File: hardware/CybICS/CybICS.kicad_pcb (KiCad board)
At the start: 2 copper layers, 160 x 100 mm, 17 parts, among them J1 Raspberry_Pi_2_3, U1 STM32G070RBTx

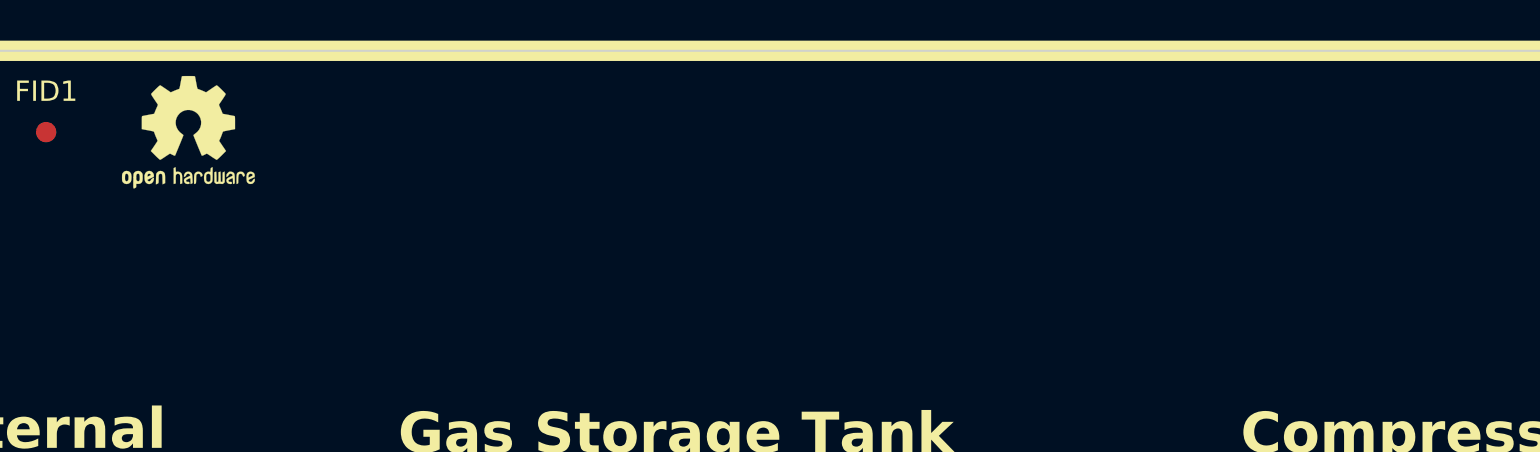
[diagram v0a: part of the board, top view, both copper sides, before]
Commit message: Fixed footprint
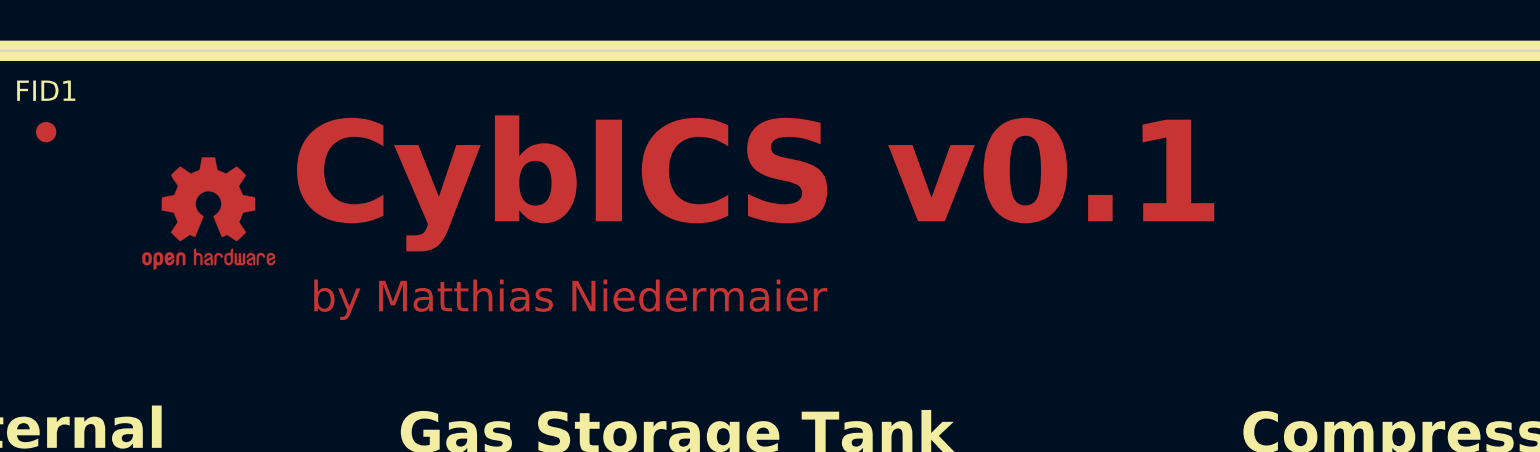
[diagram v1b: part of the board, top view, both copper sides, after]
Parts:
- moved #SYM1 4.12 mm to (66.8, 58.8)
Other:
- board text added: "CybICS v0.1"
- board text added: "by Matthias Niedermaier"

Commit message: Further development of the schematic and pcb
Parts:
- added C1: 100nF, Capacitor_SMD:C_0805_2012Metric_Pad1.18x1.45mm_HandSolder, F.Cu at (84.5, 121.5)
- added C2: 100nF, Capacitor_SMD:C_0805_2012Metric_Pad1.18x1.45mm_HandSolder, F.Cu at (105.5, 122.1)
- added C3: 4.7μF, Capacitor_SMD:C_0805_2012Metric_Pad1.18x1.45mm_HandSolder, F.Cu at (80.5, 121.5)
- added C4: 100nF, Capacitor_SMD:C_0805_2012Metric_Pad1.18x1.45mm_HandSolder, F.Cu at (81.8, 125.8)
- added D11: LED GREEN, LED_SMD:LED_1210_3225Metric_Pad1.42x2.65mm_HandSolder, F.Cu at (240.8, 123.6)
- added D12: LED GREEN, LED_SMD:LED_1210_3225Metric_Pad1.42x2.65mm_HandSolder, F.Cu at (240.8, 127.9)
- added H1: MountingHole, MountingHole:MountingHole_3.2mm_M3, F.Cu at (53.8, 53.8)
- added H2: MountingHole, MountingHole:MountingHole_3.2mm_M3, F.Cu at (207.8, 53.8)
- added H3: MountingHole, MountingHole:MountingHole_3.2mm_M3, F.Cu at (53.8, 147.8)
- added H4: MountingHole, MountingHole:MountingHole_3.2mm_M3, F.Cu at (207.8, 147.8)
- added R1: 1000R, Resistor_SMD:R_0805_2012Metric_Pad1.20x1.40mm_HandSolder, F.Cu at (111.8, 104.8)
- added R10: 1000R, Resistor_SMD:R_0805_2012Metric_Pad1.20x1.40mm_HandSolder, F.Cu at (102.8, 104.8)
- added R11: 1000R, Resistor_SMD:R_0805_2012Metric_Pad1.20x1.40mm_HandSolder, F.Cu at (235.4, 122.9)
- added R12: 1000R, Resistor_SMD:R_0805_2012Metric_Pad1.20x1.40mm_HandSolder, F.Cu at (235.4, 125.9)
- added R13: 0R, Resistor_SMD:R_0805_2012Metric_Pad1.20x1.40mm_HandSolder, F.Cu at (235.4, 128.8)
- added R14: 0R, Resistor_SMD:R_0805_2012Metric_Pad1.20x1.40mm_HandSolder, F.Cu at (235.4, 131.8)
- added R15: 0R, Resistor_SMD:R_0805_2012Metric_Pad1.20x1.40mm_HandSolder, F.Cu at (235.4, 134.7)
- added R16: 0R, Resistor_SMD:R_0805_2012Metric_Pad1.20x1.40mm_HandSolder, F.Cu at (235.4, 137.7)
- added R17: 0R, Resistor_SMD:R_0805_2012Metric_Pad1.20x1.40mm_HandSolder, F.Cu at (235.4, 140.6)
- added R2: 1000R, Resistor_SMD:R_0805_2012Metric_Pad1.20x1.40mm_HandSolder, F.Cu at (115.8, 104.8)
- added R3: 1000R, Resistor_SMD:R_0805_2012Metric_Pad1.20x1.40mm_HandSolder, F.Cu at (119.8, 104.8)
- added R4: 1000R, Resistor_SMD:R_0805_2012Metric_Pad1.20x1.40mm_HandSolder, F.Cu at (123.8, 104.8)
- added R5: 1000R, Resistor_SMD:R_0805_2012Metric_Pad1.20x1.40mm_HandSolder, F.Cu at (127.8, 104.8)
- added R6: 1000R, Resistor_SMD:R_0805_2012Metric_Pad1.20x1.40mm_HandSolder, F.Cu at (75.8, 104.8)
- added R7: 1000R, Resistor_SMD:R_0805_2012Metric_Pad1.20x1.40mm_HandSolder, F.Cu at (71.8, 104.8)
- added R8: 1000R, Resistor_SMD:R_0805_2012Metric_Pad1.20x1.40mm_HandSolder, F.Cu at (67.8, 104.8)
- added R9: 1000R, Resistor_SMD:R_0805_2012Metric_Pad1.20x1.40mm_HandSolder, F.Cu at (98.8, 104.8)
- added RV1: R_Potentiometer, Potentiometer_SMD:Potentiometer_Bourns_3314J_Vertical, F.Cu at (145.8, 107.8)
- added SW1: SW_Push, Button_Switch_SMD:SW_Push_1P1T_NO_6x6mm_H9.5mm, F.Cu at (60.8, 115.8)
- moved U1 12.4 mm to (93.8, 120.8)
- moved D5 3.94 mm to (127.6, 87.8)
- moved D4 3.81 mm to (127.6, 82.8)
- moved FID3 1.00 mm to (202.8, 54.8)
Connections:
- D1 pad 1: unconnected-(D1-K-Pad1) -> Net-(D1-K)
- D1 pad 2: unconnected-(D1-A-Pad2) -> +3V3
- D10 pad 1: unconnected-(D10-K-Pad1) -> Net-(D10-K)
- D10 pad 2: unconnected-(D10-A-Pad2) -> +3V3
- D2 pad 1: unconnected-(D2-K-Pad1) -> Net-(D2-K)
- D2 pad 2: unconnected-(D2-A-Pad2) -> +3V3
- D3 pad 1: unconnected-(D3-K-Pad1) -> Net-(D3-K)
- D3 pad 2: unconnected-(D3-A-Pad2) -> +3V3
- D4 pad 1: unconnected-(D4-K-Pad1) -> Net-(D4-K)
- D4 pad 2: unconnected-(D4-A-Pad2) -> +3V3
- D5 pad 1: unconnected-(D5-K-Pad1) -> Net-(D5-K)
- D5 pad 2: unconnected-(D5-A-Pad2) -> +3V3
- D6 pad 1: unconnected-(D6-K-Pad1) -> Net-(D6-K)
- D6 pad 2: unconnected-(D6-A-Pad2) -> +3V3
- D7 pad 1: unconnected-(D7-K-Pad1) -> Net-(D7-K)
- D7 pad 2: unconnected-(D7-A-Pad2) -> +3V3
- D8 pad 1: unconnected-(D8-K-Pad1) -> Net-(D8-K)
- D8 pad 2: unconnected-(D8-A-Pad2) -> +3V3
- D9 pad 1: unconnected-(D9-K-Pad1) -> Net-(D9-K)
- D9 pad 2: unconnected-(D9-A-Pad2) -> +3V3
- DS1 pad 1: unconnected-(DS1-VSS-Pad1) -> GND
- DS1 pad 15: unconnected-(DS1-LED(+)-Pad15) -> +3V3
- DS1 pad 16: unconnected-(DS1-LED(-)-Pad16) -> GND
- DS1 pad 2: unconnected-(DS1-VDD-Pad2) -> +3V3
- DS1 pad 3: unconnected-(DS1-VO-Pad3) -> Net-(DS1-VO)
- DS1 pad 4: unconnected-(DS1-RS-Pad4) -> /D_rs
- DS1 pad 5: unconnected-(DS1-R/W-Pad5) -> GND
- DS1 pad 6: unconnected-(DS1-E-Pad6) -> /D_enable
- J1 pad 1: unconnected-(J1-3V3-Pad1) -> +3V3
- J1 pad 12: unconnected-(J1-GPIO18/PWM0-Pad12) -> Net-(J1-GPIO18/PWM0)
- J1 pad 14: unconnected-(J1-GND-Pad14) -> GND
- J1 pad 17: unconnected-(J1-3V3-Pad17) -> +3V3
- J1 pad 18: unconnected-(J1-GPIO24-Pad18) -> Net-(J1-GPIO24)
- J1 pad 20: unconnected-(J1-GND-Pad20) -> GND
- J1 pad 22: unconnected-(J1-GPIO25-Pad22) -> Net-(J1-GPIO25)
- J1 pad 25: unconnected-(J1-GND-Pad25) -> GND
- J1 pad 3: unconnected-(J1-SDA/GPIO2-Pad3) -> Net-(J1-SDA/GPIO2)
- J1 pad 30: unconnected-(J1-GND-Pad30) -> GND
- J1 pad 34: unconnected-(J1-GND-Pad34) -> GND
- J1 pad 39: unconnected-(J1-GND-Pad39) -> GND
- J1 pad 5: unconnected-(J1-SCL/GPIO3-Pad5) -> Net-(J1-SCL/GPIO3)
- J1 pad 6: unconnected-(J1-GND-Pad6) -> GND
- J1 pad 9: unconnected-(J1-GND-Pad9) -> GND
- U1 pad 12: unconnected-(U1-NRST-Pad12) -> /STMnrst
- U1 pad 37: unconnected-(U1-PA9/NC-Pad37) -> /USART1_TX
- U1 pad 42: unconnected-(U1-PA10/NC-Pad42) -> /USART1_RX
- U1 pad 45: unconnected-(U1-PA13-Pad45) -> /SWDIO
- U1 pad 46: unconnected-(U1-PA14-Pad46) -> /SWCLK
- U1 pad 61: unconnected-(U1-PB7-Pad61) -> /I2C1_SDA
- U1 pad 62: unconnected-(U1-PB8-Pad62) -> /I2C1_SCL
- U1 pad 7: unconnected-(U1-VREF+-Pad7) -> +3V3
- U1 pad 8: unconnected-(U1-VDD-Pad8) -> +3V3
- U1 pad 9: unconnected-(U1-VSS-Pad9) -> GND
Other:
- outline, holes or cut-outs redrawn

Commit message: further development
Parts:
- added D13: LED GREEN, LED_SMD:LED_1210_3225Metric_Pad1.42x2.65mm_HandSolder, F.Cu at (55.8, 135.8)
- added D14: LED RED, LED_SMD:LED_1210_3225Metric_Pad1.42x2.65mm_HandSolder, F.Cu at (192.8, 64.8)
- added D15: LED GREEN, LED_SMD:LED_1210_3225Metric_Pad1.42x2.65mm_HandSolder, F.Cu at (192.8, 69.8)
- added D16: LED RED, LED_SMD:LED_1210_3225Metric_Pad1.42x2.65mm_HandSolder, F.Cu at (192.8, 87.8)
- added D17: LED GREEN, LED_SMD:LED_1210_3225Metric_Pad1.42x2.65mm_HandSolder, F.Cu at (192.8, 82.8)
- added D18: LED RED, LED_SMD:LED_1210_3225Metric_Pad1.42x2.65mm_HandSolder, F.Cu at (180.8, 108.8)
- added D19: LED GREEN, LED_SMD:LED_1210_3225Metric_Pad1.42x2.65mm_HandSolder, F.Cu at (180.8, 103.8)
- added J2: Conn_01x03_Pin, Connector_PinHeader_2.54mm:PinHeader_1x03_P2.54mm_Vertical, F.Cu at (108.3, 129.8)
- added J3: Conn_01x05_Pin, Connector_PinHeader_2.54mm:PinHeader_1x05_P2.54mm_Vertical, F.Cu at (67.8, 124.9)
- added R18: 0R, Resistor_SMD:R_0805_2012Metric_Pad1.20x1.40mm_HandSolder, F.Cu at (77.8, 135.8)
- added R19: 0R, Resistor_SMD:R_0805_2012Metric_Pad1.20x1.40mm_HandSolder, F.Cu at (81.8, 135.8)
- added R20: 100R, Resistor_SMD:R_0805_2012Metric_Pad1.20x1.40mm_HandSolder, F.Cu at (60.8, 135.8)
- added R21: 100R, Resistor_SMD:R_0805_2012Metric_Pad1.20x1.40mm_HandSolder, F.Cu at (122.8, 105.8)
- added R22: 100R, Resistor_SMD:R_0805_2012Metric_Pad1.20x1.40mm_HandSolder, F.Cu at (122.8, 109.8)
- added R23: 100R, Resistor_SMD:R_0805_2012Metric_Pad1.20x1.40mm_HandSolder, F.Cu at (122.8, 117.8)
- added R24: 100R, Resistor_SMD:R_0805_2012Metric_Pad1.20x1.40mm_HandSolder, F.Cu at (122.8, 113.8)
- added R25: 100R, Resistor_SMD:R_0805_2012Metric_Pad1.20x1.40mm_HandSolder, F.Cu at (122.8, 125.8)
- added R26: 100R, Resistor_SMD:R_0805_2012Metric_Pad1.20x1.40mm_HandSolder, F.Cu at (122.8, 121.8)
- added R27: 1kR, Resistor_SMD:R_0805_2012Metric_Pad1.20x1.40mm_HandSolder, F.Cu at (63.8, 104.8)
- added SW2: SW_Push, Button_Switch_THT:SW_PUSH_6mm_H5mm, F.Cu at (54.3, 94.3)
- R1, R10, R11, R12, R2, R3, R4, R5, R6, R7, R8, R9: value 1000R -> 100R
- SW1: footprint Button_Switch_SMD:SW_Push_1P1T_NO_6x6mm_H9.5mm -> Button_Switch_THT:SW_PUSH_6mm_H5mm
- moved D12 185.0 mm to (55.8, 130.8), turned to 180 degrees
- moved D11 185.0 mm to (55.8, 125.8), turned to 180 degrees
- moved R12 174.7 mm to (60.8, 130.8), turned to 180 degrees
- moved R11 174.6 mm to (60.8, 125.8), turned to 180 degrees
- moved R16 165.6 mm to (69.8, 135.8), turned to 90 degrees
- moved R17 161.7 mm to (73.8, 135.8), turned to 90 degrees
- moved R13 149.8 mm to (85.8, 135.8), turned to -90 degrees
- moved R14 145.7 mm to (89.8, 135.8), turned to -90 degrees
- moved R15 141.6 mm to (93.8, 135.8), turned to 90 degrees
- moved R1 24.0 mm to (87.8, 104.8)
- moved R2 24.0 mm to (91.8, 104.8)
- moved R3 24.0 mm to (95.8, 104.8)
- moved R4 24.0 mm to (99.8, 104.8)
- moved R5 24.0 mm to (103.8, 104.8)
- moved C2 22.3 mm to (83.8, 116.8), turned to 90 degrees
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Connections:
- DS1 pad 11: unconnected-(DS1-D4-Pad11) -> /D_d4
- DS1 pad 12: unconnected-(DS1-D5-Pad12) -> /D_d5
- DS1 pad 13: unconnected-(DS1-D6-Pad13) -> /D_d6
- DS1 pad 14: unconnected-(DS1-D7-Pad14) -> /D_d7
- J1 pad 10: unconnected-(J1-GPIO15/RXD-Pad10) -> Net-(J1-GPIO15/RXD)
- J1 pad 8: unconnected-(J1-GPIO14/TXD-Pad8) -> Net-(J1-GPIO14/TXD)
- R1 pad 1: unconnected-(R1-Pad1) -> /PD6
- R10 pad 1: unconnected-(R10-Pad1) -> /PB3
- R2 pad 1: unconnected-(R2-Pad1) -> /PD5
- R3 pad 1: unconnected-(R3-Pad1) -> /PD4
- R4 pad 1: unconnected-(R4-Pad1) -> /PD3
- R5 pad 1: unconnected-(R5-Pad1) -> /PD2
- R6 pad 1: unconnected-(R6-Pad1) -> /PB5
- R7 pad 1: unconnected-(R7-Pad1) -> /PB6
- R8 pad 1: unconnected-(R8-Pad1) -> /PB9
- R9 pad 1: unconnected-(R9-Pad1) -> /PB4
- U1 pad 30: unconnected-(U1-PB10-Pad30) -> /D_enable
- U1 pad 31: unconnected-(U1-PB11-Pad31) -> /D_rs
- U1 pad 32: unconnected-(U1-PB12-Pad32) -> /D_d4
- U1 pad 33: unconnected-(U1-PB13-Pad33) -> /D_d5
- U1 pad 34: unconnected-(U1-PB14-Pad34) -> /D_d6
- U1 pad 35: unconnected-(U1-PB15-Pad35) -> /D_d7
- U1 pad 52: unconnected-(U1-PD2-Pad52) -> /PD2
- U1 pad 53: unconnected-(U1-PD3-Pad53) -> /PD3
- U1 pad 54: unconnected-(U1-PD4-Pad54) -> /PD4
- U1 pad 55: unconnected-(U1-PD5-Pad55) -> /PD5
- U1 pad 56: unconnected-(U1-PD6-Pad56) -> /PD6
- U1 pad 57: unconnected-(U1-PB3-Pad57) -> /PB3
- U1 pad 58: unconnected-(U1-PB4-Pad58) -> /PB4
- U1 pad 59: unconnected-(U1-PB5-Pad59) -> /PB5
- U1 pad 60: unconnected-(U1-PB6-Pad60) -> /PB6
- U1 pad 63: unconnected-(U1-PB9-Pad63) -> /PB9
- U1 pad 64: unconnected-(U1-PC10-Pad64) -> /PC10
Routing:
- net Net-(D14-K): track 0.00 -> 85.1 mm, vias 0 -> 2
- net Net-(D15-K): track 0.00 -> 84.1 mm, vias 0 -> 2
- net Net-(D17-K): track 0.00 -> 80.4 mm, vias 0 -> 2
- net Net-(D16-K): track 0.00 -> 79.9 mm, vias 0 -> 2
- net Net-(D6-K): track 0.00 -> 79.3 mm, vias 0 -> 2
- net Net-(D7-K): track 0.00 -> 74.2 mm, vias 0 -> 2
- net Net-(D18-K): track 0.00 -> 70.5 mm, vias 0 -> 2
- net Net-(D8-K): track 0.00 -> 67.2 mm, vias 0 -> 2
- net Net-(D19-K): track 0.00 -> 65.6 mm, vias 0 -> 2
- net Net-(D9-K): track 0.00 -> 61.1 mm, vias 0 -> 2
- net Net-(D10-K): track 0.00 -> 57.5 mm, vias 0 -> 2
- net Net-(D4-K): track 0.00 -> 56.8 mm, vias 0 -> 2
- net /PC10: track 0.00 -> 56.3 mm
- net Net-(D5-K): track 0.00 -> 50.3 mm, vias 0 -> 2
- net /I2C1_SDA: track 0.00 -> 35.9 mm, vias 0 -> 3
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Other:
- board text added: "3.3V"
- board text added: "GND"
- board text added: "GND TX RX"
- board text added: "SWCLK"
- board text added: "SWDIO"
- board text added: "System Valve"
- board text added: "nRST"

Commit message: Update on schematic and PCB
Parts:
- removed #SYM1: OSHW-Logo2_7.3x6mm_SilkScreen, Symbol:OSHW-Logo2_7.3x6mm_SilkScreen
- removed H4: MountingHole, MountingHole:MountingHole_3.2mm_M3
- added REF**: OSHW-Logo2_14.6x12mm_Copper, Symbol:OSHW-Logo2_14.6x12mm_Copper, F.Cu at (70.8, 58.8)
- DS1: value WC1602A / HD44780 -> WC1602A/HD44780
- moved R21 6.00 mm to (116.8, 105.8)
- moved R22 6.00 mm to (116.8, 109.8)
- moved R23 6.00 mm to (116.8, 117.8)
- moved R24 6.00 mm to (116.8, 113.8)
- moved R25 6.00 mm to (116.8, 125.8)
- moved R26 6.00 mm to (116.8, 121.8)
- moved J2 5.58 mm to (110.8, 124.8)
- turned R15 to -90 degrees
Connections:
- J1 pad 24: unconnected-(J1-~{CE0}/GPIO8-Pad24) -> /PA0
- J1 pad 26: unconnected-(J1-~{CE1}/GPIO7-Pad26) -> /PA1
- J1 pad 28: unconnected-(J1-ID_SC/GPIO1-Pad28) -> /PA2
- J1 pad 32: unconnected-(J1-PWM0/GPIO12-Pad32) -> /PA3
- J1 pad 36: unconnected-(J1-GPIO16-Pad36) -> /PA4
- J1 pad 38: unconnected-(J1-GPIO20/MOSI1-Pad38) -> /PA5
- J1 pad 40: unconnected-(J1-GPIO21/SCLK1-Pad40) -> /PA6
- J1 pad 7: unconnected-(J1-GCLK0/GPIO4-Pad7) -> /RP_heartbeat
- R11 pad 1: unconnected-(R11-Pad1) -> /ST_heartbeat
- R12 pad 1: unconnected-(R12-Pad1) -> /RP_heartbeat
- R21 pad 1: unconnected-(R21-Pad1) -> /PD1
- R22 pad 1: unconnected-(R22-Pad1) -> /PD0
- R23 pad 1: unconnected-(R23-Pad1) -> /PC8
- R24 pad 1: unconnected-(R24-Pad1) -> /PC9
- R25 pad 1: unconnected-(R25-Pad1) -> /PA12
- R26 pad 1: unconnected-(R26-Pad1) -> /PA15
- U1 pad 16: unconnected-(U1-PC3-Pad16) -> /ST_heartbeat
- U1 pad 17: unconnected-(U1-PA0-Pad17) -> /PA0
- U1 pad 18: unconnected-(U1-PA1-Pad18) -> /PA1
- U1 pad 19: unconnected-(U1-PA2-Pad19) -> /PA2
- U1 pad 20: unconnected-(U1-PA3-Pad20) -> /PA3
- U1 pad 21: unconnected-(U1-PA4-Pad21) -> /PA4
- U1 pad 22: unconnected-(U1-PA5-Pad22) -> /PA5
- U1 pad 23: unconnected-(U1-PA6-Pad23) -> /PA6
- U1 pad 44: unconnected-(U1-PA12/PA10-Pad44) -> /PA12
- U1 pad 47: unconnected-(U1-PA15-Pad47) -> /PA15
- U1 pad 48: unconnected-(U1-PC8-Pad48) -> /PC8
- U1 pad 49: unconnected-(U1-PC9-Pad49) -> /PC9
- U1 pad 50: unconnected-(U1-PD0-Pad50) -> /PD0
- U1 pad 51: unconnected-(U1-PD1-Pad51) -> /PD1
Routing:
- net /D_d7: track 0.00 -> 79.0 mm, vias 0 -> 2
- net /D_d6: track 0.00 -> 77.7 mm, vias 0 -> 2
- net /D_d5: track 0.00 -> 76.6 mm, vias 0 -> 2
- net /D_d4: track 0.00 -> 75.0 mm, vias 0 -> 2
- net /D_enable: track 0.00 -> 65.5 mm
- net /D_rs: track 0.00 -> 58.8 mm
- net /SWCLK: track 0.00 -> 56.7 mm, vias 0 -> 3
- net /SWDIO: track 0.00 -> 51.5 mm, vias 0 -> 3
- net /STMnrst: track 0.00 -> 49.0 mm
- net /USART1_RX: track 17.3 -> 51.0 mm, vias 0 -> 1
- net /PA6: track 0.00 -> 32.2 mm
- net /RP_heartbeat: track 0.00 -> 31.5 mm
- net /PA5: track 0.00 -> 30.2 mm
- net /USART1_TX: track 12.8 -> 42.1 mm, vias 0 -> 1
- net /ST_heartbeat: track 0.00 -> 28.5 mm, vias 0 -> 2
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- added copper zone on F.Cu, net +3V3
- added copper zone on B.Cu, net GND
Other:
- outline, holes or cut-outs redrawn
- board text added: "Matthias Niedermaier"
- board text removed: "by Matthias Niedermaier"
